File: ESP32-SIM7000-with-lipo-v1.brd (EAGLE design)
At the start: 90 x 60 mm, 75 parts, among them IC2 TXB0104, Q1 BSS138L, Q2 BSS138L, Q3 9013, Q5 9013, U3 ESP-WROOM-32, U4 MCP73831T-2ACI/OT, X1 LTE-uFL

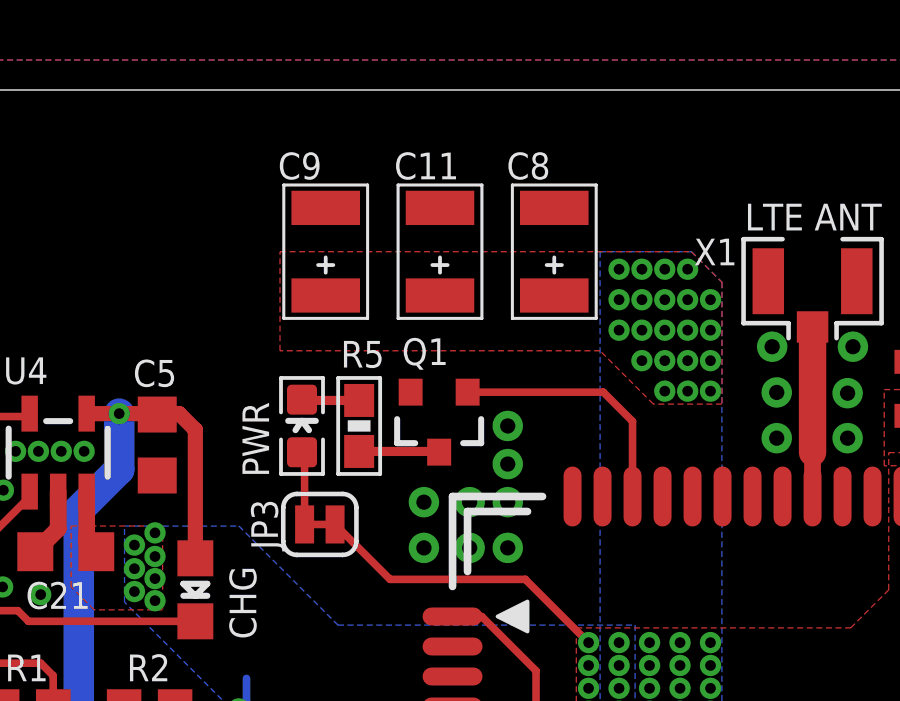
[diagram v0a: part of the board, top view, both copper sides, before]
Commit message: change caps package
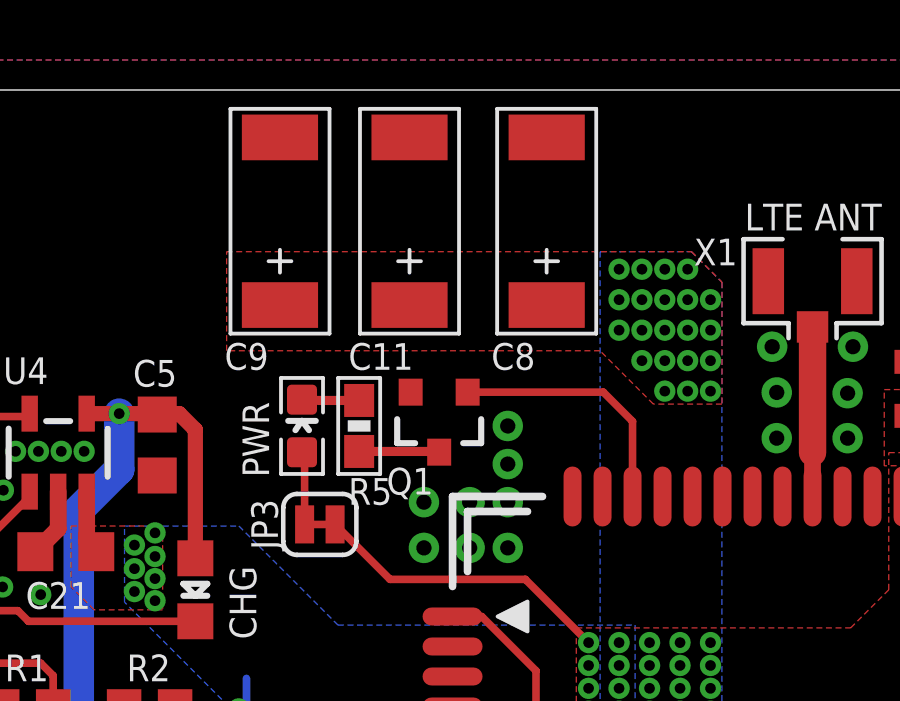
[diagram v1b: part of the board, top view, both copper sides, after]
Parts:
- C11, C8, C9: device discrete:AVX_B -> discrete:AVX_C
- moved C9 1.83 mm to (49.3, 55.6)
- moved C11 1.44 mm to (53.6, 55.6)
- moved C8 1.05 mm to (58.2, 55.6)
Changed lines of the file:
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@@
 </element>
 <element name="R5" library="TimWoo-Resistors" library_urn="urn:adsk.eagle:library:500711" package="0603-RES-MARKED" package3d_urn="urn:adsk.eagle:package:500751/2" value="2k" x="51.9154" y="48.801" smashed="yes" rot="R90">
-<attribute name="NAME" x="51.3004" y="50.747" size="0.889" layer="25" font="vector"/>
+<attribute name="NAME" x="51.5544" y="46.175" size="0.889" layer="25" font="vector"/>
 <attribute name="VALUE" x="53.1854" y="47.785" size="0.4064" layer="27" font="vector" ratio="16" rot="R90"/>
 </element>
@@
 </element>
 <element name="Q1" library="TimWoo-MOSFETs" library_urn="urn:adsk.eagle:library:501962" package="SOT23-3" package3d_urn="urn:adsk.eagle:package:501973/2" value="BSS138L" x="54.5824" y="48.928" smashed="yes" rot="R180">
-<attribute name="NAME" x="54.8999" y="51.722" size="0.889" layer="25" font="vector" rot="R180"/>
+<attribute name="NAME" x="54.3919" y="47.404" size="0.889" layer="25" font="vector" rot="R180"/>
 <attribute name="VALUE" x="55.5984" y="49.1185" size="0.4064" layer="27" rot="R180"/>
 </element>
@@
 <attribute name="VALUE" x="73.279" y="50.038" size="0.6096" layer="27" font="vector" ratio="20" rot="R90" align="top-center"/>
 </element>
-<element name="C8" library="discrete" package="AVX_B" value="220uF/6.3V" x="58.42" y="54.61" smashed="yes" rot="R90">
-<attribute name="NAME" x="58.293" y="57.912" size="0.889" layer="25" font="vector" ratio="10" rot="R180"/>
-<attribute name="VALUE" x="59.69" y="52.705" size="0.8128" layer="27" ratio="10" rot="R90"/>
-</element>
-<element name="C9" library="discrete" package="AVX_B" value="220uF/6.3V" x="50.8" y="54.61" smashed="yes" rot="R90">
-<attribute name="NAME" x="50.673" y="57.912" size="0.889" layer="25" font="vector" ratio="10" rot="R180"/>
-<attribute name="VALUE" x="52.07" y="52.705" size="0.8128" layer="27" ratio="10" rot="R90"/>
-</element>
-<element name="C11" library="discrete" package="AVX_B" value="220uF/6.3V" x="54.61" y="54.61" smashed="yes" rot="R90">
-<attribute name="NAME" x="55.245" y="57.912" size="0.889" layer="25" font="vector" ratio="10" rot="R180"/>
-<attribute name="VALUE" x="55.88" y="52.705" size="0.8128" layer="27" ratio="10" rot="R90"/>
+<element name="C8" library="discrete" package="AVX_C" value="220uF/6.3V" x="58.166" y="55.626" smashed="yes" rot="R90">
+<attribute name="NAME" x="57.785" y="51.562" size="0.889" layer="25" font="vector" ratio="10" rot="R180"/>
+<attribute name="VALUE" x="59.436" y="53.721" size="0.8128" layer="27" ratio="10" rot="R90"/>
+</element>
+<element name="C9" library="discrete" package="AVX_C" value="220uF/6.3V" x="49.276" y="55.626" smashed="yes" rot="R90">
+<attribute name="NAME" x="48.895" y="51.562" size="0.889" layer="25" font="vector" ratio="10" rot="R180"/>
+<attribute name="VALUE" x="50.546" y="53.721" size="0.8128" layer="27" ratio="10" rot="R90"/>
+</element>
+<element name="C11" library="discrete" package="AVX_C" value="220uF/6.3V" x="53.594" y="55.626" smashed="yes" rot="R90">
+<attribute name="NAME" x="53.721" y="51.562" size="0.889" layer="25" font="vector" ratio="10" rot="R180"/>
+<attribute name="VALUE" x="54.864" y="53.721" size="0.8128" layer="27" ratio="10" rot="R90"/>
 </element>
 </elements>
@@
 <wire x1="52.9434" y1="43.688" x2="51.1124" y2="45.519" width="0.254" layer="1"/>
 <polygon width="0.254" layer="1">
-<vertex x="49.276" y="54.61"/>
+<vertex x="47.498" y="54.61"/>
 <vertex x="62.992" y="54.61"/>
 <vertex x="64.008" y="53.594"/>
@@
 <vertex x="61.722" y="49.53"/>
 <vertex x="59.944" y="51.308"/>
-<vertex x="49.276" y="51.308"/>
+<vertex x="47.498" y="51.308"/>
 </polygon>
 <polygon width="0.254" layer="16">
